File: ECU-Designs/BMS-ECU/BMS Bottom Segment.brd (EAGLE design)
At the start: 130 x 110 mm, 90 parts, among them Q10 P-CHANNEL_MOSFET_DMP3099L-7, Q11 P-CHANNEL_MOSFET_DMP3099L-7, Q12 P-CHANNEL_MOSFET_DMP3099L-7, Q13 NPN_BCP56T1, Q3 P-CHANNEL_MOSFET_DMP3099L-7, Q4 P-CHANNEL_MOSFET_DMP3099L-7, Q5 P-CHANNEL_MOSFET_DMP3099L-7, Q6 P-CHANNEL_MOSFET_DMP3099L-7, Q8 P-CHANNEL_MOSFET_DMP3099L-7, Q9 P-CHANNEL_MOSFET_DMP3099L-7

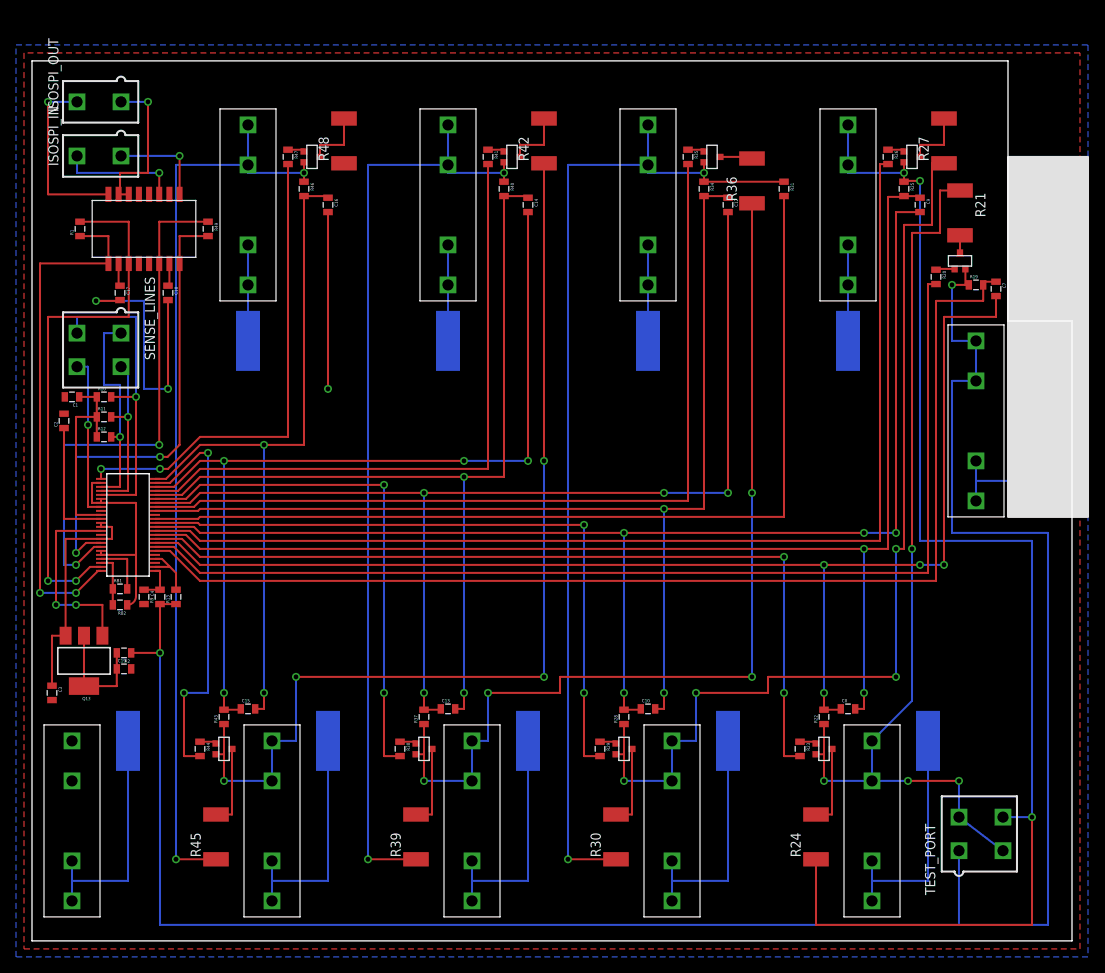
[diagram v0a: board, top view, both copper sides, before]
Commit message: Added mounting holes to BMS segment boards
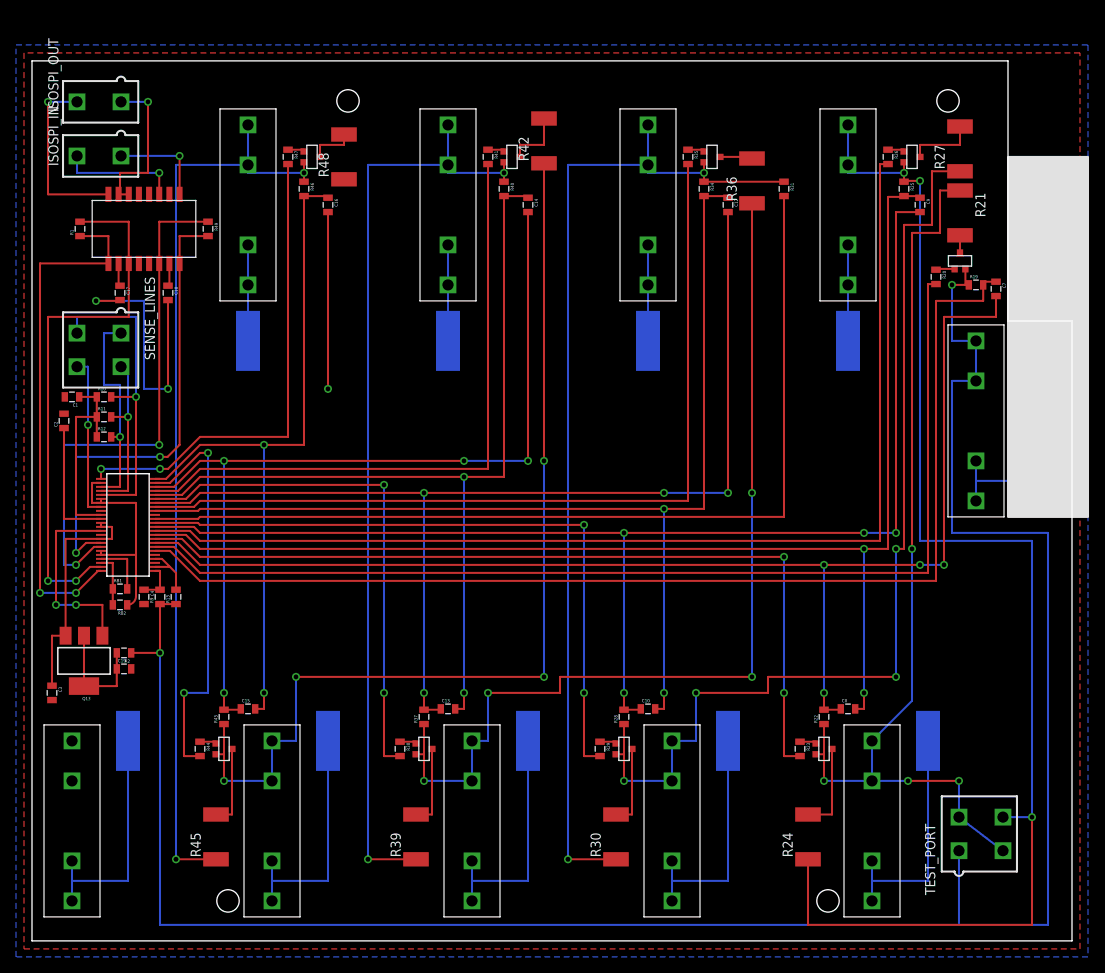
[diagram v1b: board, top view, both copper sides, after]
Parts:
- moved R27 2.24 mm to (116.0, 94.0)
- moved R48 2.00 mm to (39.0, 93.0)
- moved R24 1.00 mm to (97.0, 8.00)
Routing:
- net N$66: track 7.80 -> 5.80 mm
- net N$30: track 7.80 -> 8.80 mm
- net N$25: track 10.2 -> 11.2 mm
- net CELL4: track 125.3 -> 126.3 mm
- net CELL3: track 163.4 -> 164.4 mm
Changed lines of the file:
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@@
 <layer number="43" name="vRestrict" color="2" fill="10" visible="yes" active="yes"/>
 <layer number="44" name="Drills" color="7" fill="1" visible="no" active="yes"/>
-<layer number="45" name="Holes" color="7" fill="1" visible="no" active="yes"/>
+<layer number="45" name="Holes" color="7" fill="1" visible="yes" active="yes"/>
 <layer number="46" name="Milling" color="3" fill="1" visible="no" active="yes"/>
 <layer number="47" name="Measures" color="7" fill="1" visible="no" active="yes"/>
@@
 <dimension x1="-2" y1="105" x2="-2" y2="-5" x3="-4" y3="50" textsize="1.778" layer="20"/>
 <dimension x1="0" y1="107" x2="130" y2="107" x3="65" y3="110" textsize="1.778" layer="20"/>
+<hole x="39.5" y="100" drill="2.8"/>
+<hole x="24.5" y="0" drill="2.8"/>
+<hole x="99.5" y="0" drill="2.8"/>
+<hole x="114.5" y="100" drill="2.8"/>
 </plain>
 <attributes>
@@
 <element name="R22" library="HyTechDevices" package="0805" value="100Ω" x="99" y="23" rot="R90"/>
 <element name="R23" library="HyTechDevices" package="0805" value="3.3kΩ" x="96" y="19" rot="R270"/>
-<element name="R24" library="HyTechDevices" package="R2512" value="33Ω" x="98" y="8" rot="R90"/>
+<element name="R24" library="HyTechDevices" package="R2512" value="33Ω" x="97" y="8" rot="R90"/>
 <element name="R25" library="HyTechDevices" package="0805" value="100Ω" x="109" y="89" rot="R270"/>
 <element name="R26" library="HyTechDevices" package="0805" value="3.3kΩ" x="107" y="93" rot="R270"/>
-<element name="R27" library="HyTechDevices" package="R2512" value="33Ω" x="114" y="95" rot="R90"/>
+<element name="R27" library="HyTechDevices" package="R2512" value="33Ω" x="116" y="94" rot="R90"/>
 <element name="R28" library="HyTechDevices" package="0805" value="100Ω" x="74" y="23" rot="R90"/>
 <element name="R29" library="HyTechDevices" package="0805" value="3.3kΩ" x="71" y="19" rot="R270"/>
@@
 <element name="R46" library="HyTechDevices" package="0805" value="100Ω" x="34" y="89" rot="R270"/>
 <element name="R47" library="HyTechDevices" package="0805" value="3.3kΩ" x="32" y="93" rot="R270"/>
-<element name="R48" library="HyTechDevices" package="R2512" value="33Ω" x="39" y="95" rot="R90"/>
+<element name="R48" library="HyTechDevices" package="R2512" value="33Ω" x="39" y="93" rot="R90"/>
 <element name="R49" library="HyTechDevices" package="0805" value="120Ω" x="22" y="84" rot="R270"/>
 <element name="R9" library="HyTechDevices" package="0805" value="100Ω" x="16" y="38" rot="R90"/>
@@
 <contactref element="Q4" pad="3"/>
 <wire x1="100" y1="19" x2="100" y2="10.8" width="0.254" layer="1"/>
-<wire x1="100" y1="10.8" x2="98" y2="10.8" width="0.254" layer="1"/>
+<wire x1="100" y1="10.8" x2="97" y2="10.8" width="0.254" layer="1"/>
 </signal>
 <signal name="CELL2">
@@
 <contactref element="Q5" pad="3"/>
 <wire x1="111" y1="93" x2="111" y2="94.5" width="0.254" layer="1"/>
-<wire x1="111" y1="94.5" x2="114" y2="94.5" width="0.254" layer="1"/>
-<wire x1="114" y1="94.5" x2="114" y2="97.8" width="0.254" layer="1"/>
+<wire x1="111" y1="94.5" x2="116" y2="94.5" width="0.254" layer="1"/>
+<wire x1="116" y1="94.5" x2="116" y2="96.8" width="0.254" layer="1"/>
 </signal>
 <signal name="C8">
@@
 <wire x1="102" y1="92" x2="102" y2="97" width="0.254" layer="16"/>
 <wire x1="109" y1="92.325" x2="109" y2="91" width="0.254" layer="1"/>
-<wire x1="98" y1="5.2" x2="98" y2="-3" width="0.254" layer="1"/>
-<wire x1="98" y1="-3" x2="125" y2="-3" width="0.254" layer="1"/>
+<wire x1="97" y1="5.2" x2="97" y2="-3" width="0.254" layer="1"/>
+<wire x1="97" y1="-3" x2="125" y2="-3" width="0.254" layer="1"/>
 <wire x1="125" y1="-3" x2="125" y2="10.47" width="0.254" layer="1"/>
 <via x="125" y="10.47" extent="1-16" drill="0.6"/>
@@
 <via x="74" y="15" extent="1-16" drill="0.6"/>
 <wire x1="74" y1="15" x2="80" y2="15" width="0.254" layer="16"/>
-<wire x1="114" y1="92.2" x2="112.5" y2="92.2" width="0.254" layer="1"/>
-<wire x1="112.5" y1="92.2" x2="112.5" y2="84.5" width="0.254" layer="1"/>
+<wire x1="116" y1="91.2" x2="112.5" y2="91.2" width="0.254" layer="1"/>
+<wire x1="112.5" y1="91.2" x2="112.5" y2="84.5" width="0.254" layer="1"/>
 <wire x1="112.5" y1="84.5" x2="109" y2="84.5" width="0.254" layer="1"/>
 <wire x1="108" y1="28" x2="92" y2="28" width="0.254" layer="1"/>
@@
 <wire x1="36" y1="93" x2="36" y2="94.5" width="0.254" layer="1"/>
 <wire x1="36" y1="94.5" x2="39" y2="94.5" width="0.254" layer="1"/>
-<wire x1="39" y1="94.5" x2="39" y2="97.8" width="0.254" layer="1"/>
+<wire x1="39" y1="94.5" x2="39" y2="95.8" width="0.254" layer="1"/>
 </signal>
 <signal name="N$15">
